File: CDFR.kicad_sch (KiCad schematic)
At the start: 11 parts, among them J1 Conn_01x03, J2 Conn_01x03, J3 Conn_01x03, J4 Conn_01x03, J5 Conn_01x03, J6 Conn_01x02_Socket, J7 Screw_Terminal_01x02, U1 RASPBERRY_PI_3_MODEL_B_, U2 YAAJ_DCDC_StepDown_LM2596

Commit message: Add files via upload
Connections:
- net GND: now also J7.2 (Pin_2), U2.2 (GND)
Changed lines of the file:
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@@
 (kicad_sch (version 20230121) (generator eeschema)
   (paper "A4")
+  (junction (at 167.64 81.28) (diameter 0) (color 0 0 0 0)
+  )
   (junction (at 60.96 73.66) (diameter 0) (color 0 0 0 0)
   )
@@
   )
   (junction (at 72.39 73.66) (diameter 0) (color 0 0 0 0)
+  )
+  (junction (at 162.56 81.28) (diameter 0) (color 0 0 0 0)
   )
   (junction (at 151.13 129.54) (diameter 0) (color 0 0 0 0)
@@
     (stroke (width 0) (type default))
   )
+  (wire (pts (xy 162.56 81.28) (xy 167.64 81.28))
+    (stroke (width 0) (type default))
+  )

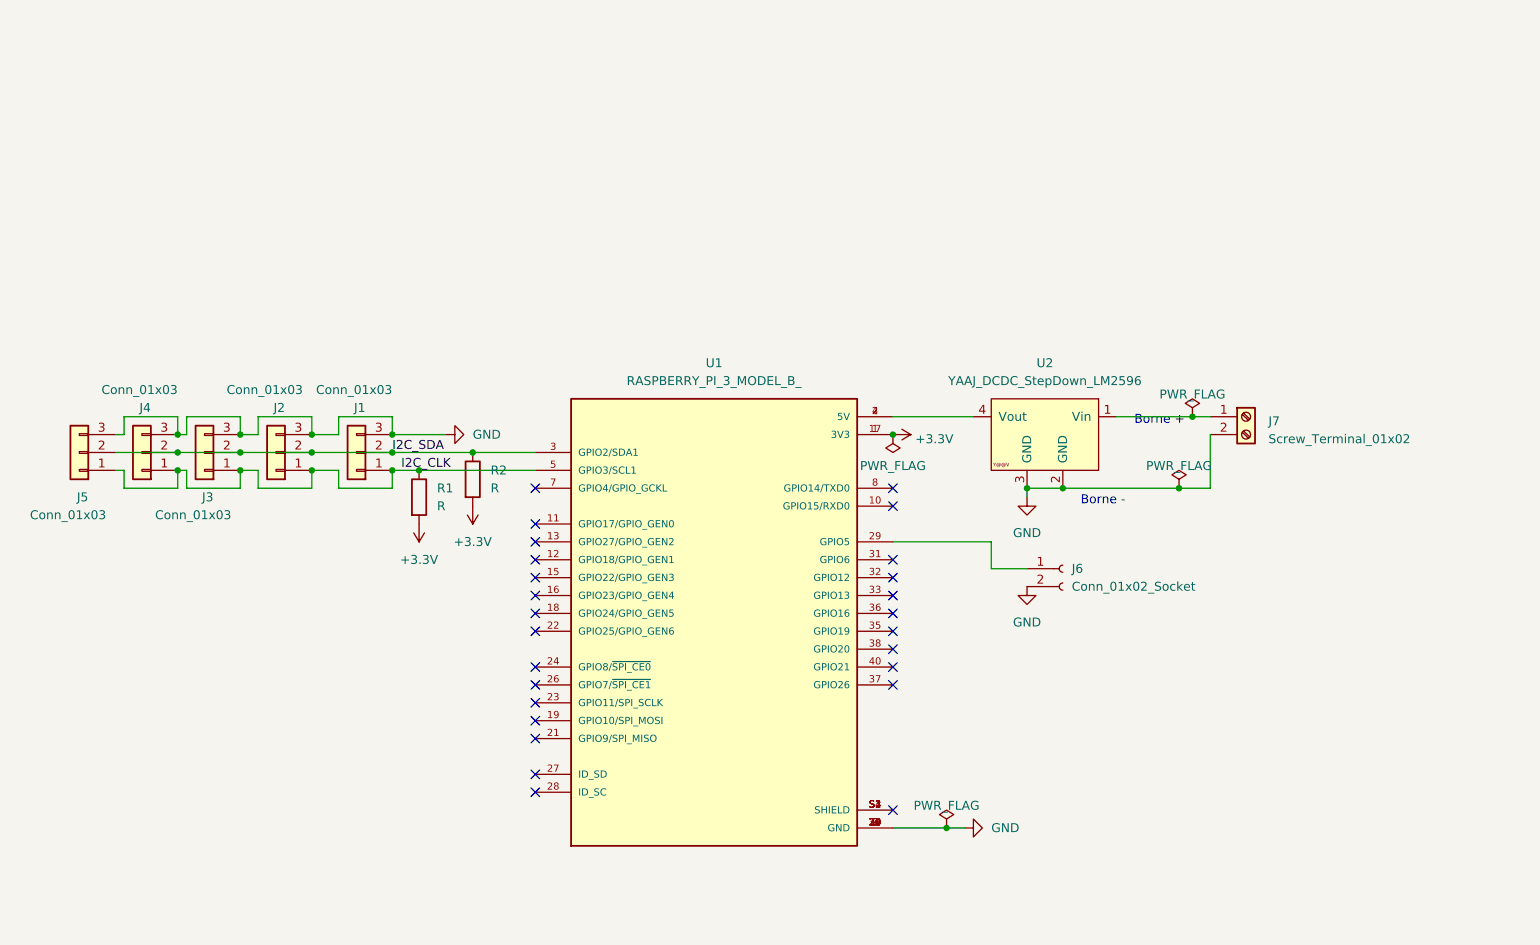
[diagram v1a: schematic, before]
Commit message: ajout lidar et antiRerse voltage
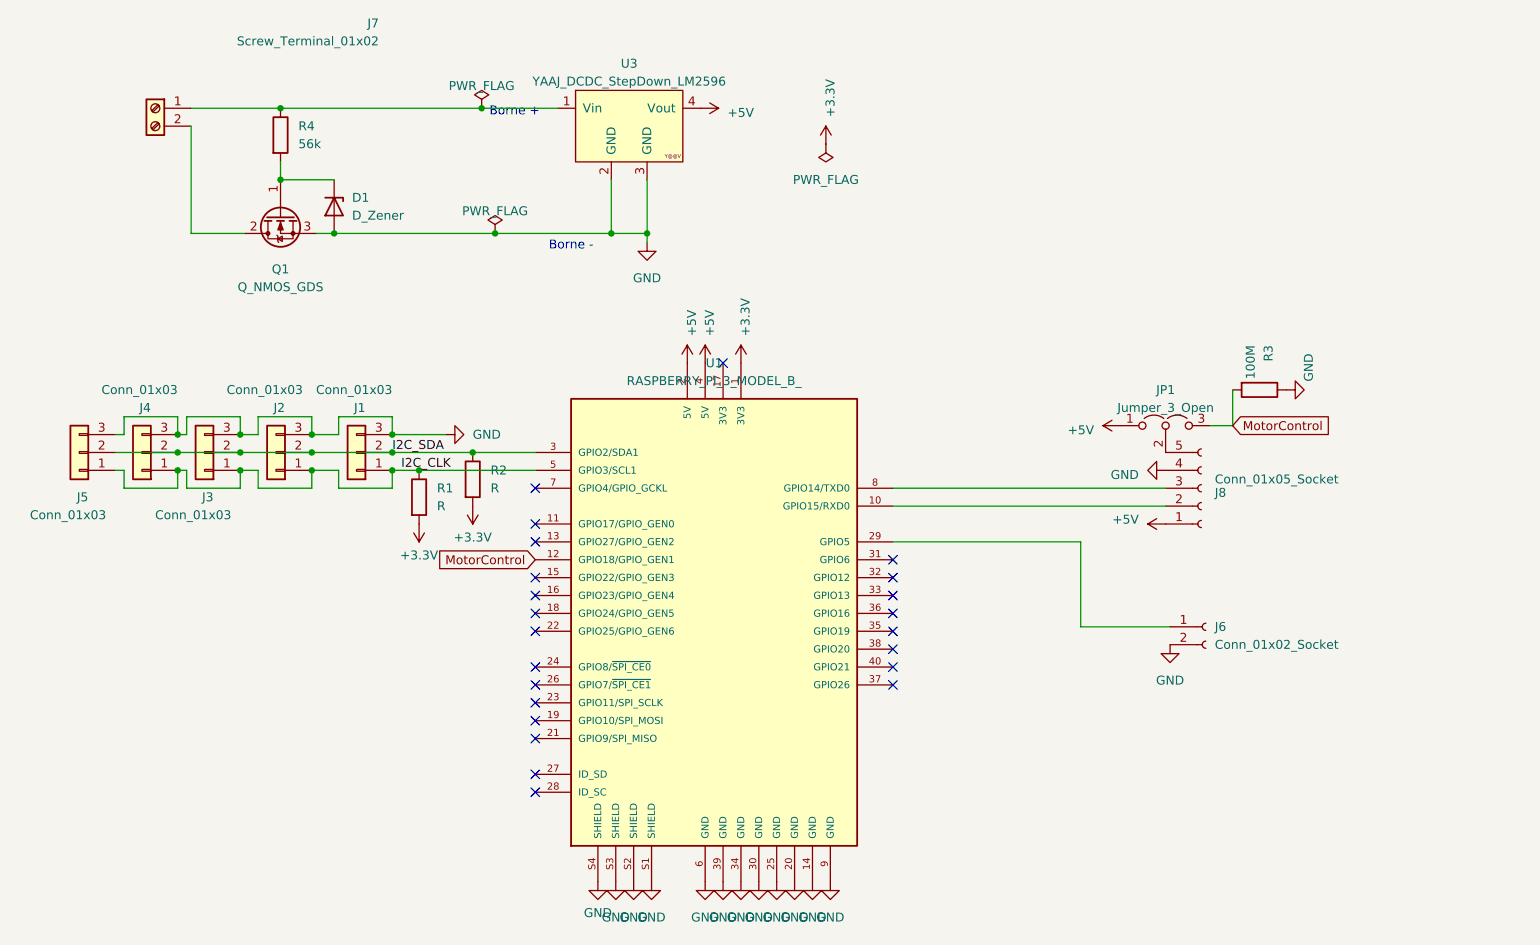
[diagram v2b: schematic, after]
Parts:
- removed U2: YAAJ_DCDC_StepDown_LM2596, emprient2:YAAJ_DCDC_StepDown_LM2596, symbol yaaj_dcdc_stepdown_lm2596:YAAJ_DCDC_StepDown_LM2596
- added D1: D_Zener, Diode_SMD:D_SOD-123, symbol Device:D_Zener
- added J8: Conn_01x05_Socket, Connector_JST:JST_XH_B5B-XH-A_1x05_P2.50mm_Vertical, symbol Connector:Conn_01x05_Socket
- added JP1: Jumper_3_Open, Connector_PinHeader_2.54mm:PinHeader_1x03_P2.54mm_Vertical, symbol Jumper:Jumper_3_Open
- added Q1: Q_NMOS_GDS, Package_TO_SOT_SMD:TO-252-2, symbol Device:Q_NMOS_GDS
- added R3: 100M, Resistor_SMD:R_0805_2012Metric, symbol Device:R
- added R4: 56k, Resistor_SMD:R_0805_2012Metric_Pad1.20x1.40mm_HandSolder, symbol Device:R
- added U3: YAAJ_DCDC_StepDown_LM2596, LM2596:YAAJ_DCDC_StepDown_LM2596, symbol yaaj_dcdc_stepdown_lm2596:YAAJ_DCDC_StepDown_LM2596
- U1: footprint emprient:MODULE_RASPBERRY_PI_3_MODEL_B_ -> raspberryPi:EmpreintPourShiel_RaspberryPi3B
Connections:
- net +3.3V: no longer U1.17 (3V3)
- net GND: now also U1.S1 (SHIELD), U1.S2 (SHIELD), U1.S3 (SHIELD), U1.S4 (SHIELD), D1.2 (A), J8.4 (Pin_4), Q1.3 (S), R3.1, U3.2 (GND), U3.3 (GND); no longer J7.2 (Pin_2)
- net at J7.1 (Pin_1): now also R4.1, U3.1 (Vin)
- net +5V: now reaches U1.2 (5V), U1.4 (5V)
- net +5V: now also J8.1 (Pin_1), JP1.1 (A), U3.4 (Vout)
- net at U1.10 (GPIO15/RXD0): now also J8.2 (Pin_2)
- net MotorControl: now reaches U1.12 (GPIO18/GPIO_GEN1)
- net MotorControl: now also JP1.3 (B), R3.2
- net at U1.8 (GPIO14/TXD0): now also J8.3 (Pin_3)
- new net: J8.5 (Pin_5), JP1.2 (C)
- new net: D1.1 (K), Q1.1 (G), R4.2
- new net: J7.2 (Pin_2), Q1.2 (D)
- no-connect marks 26 -> 23
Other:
- moved on the sheet: J6, J7

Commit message: ajout i2c power
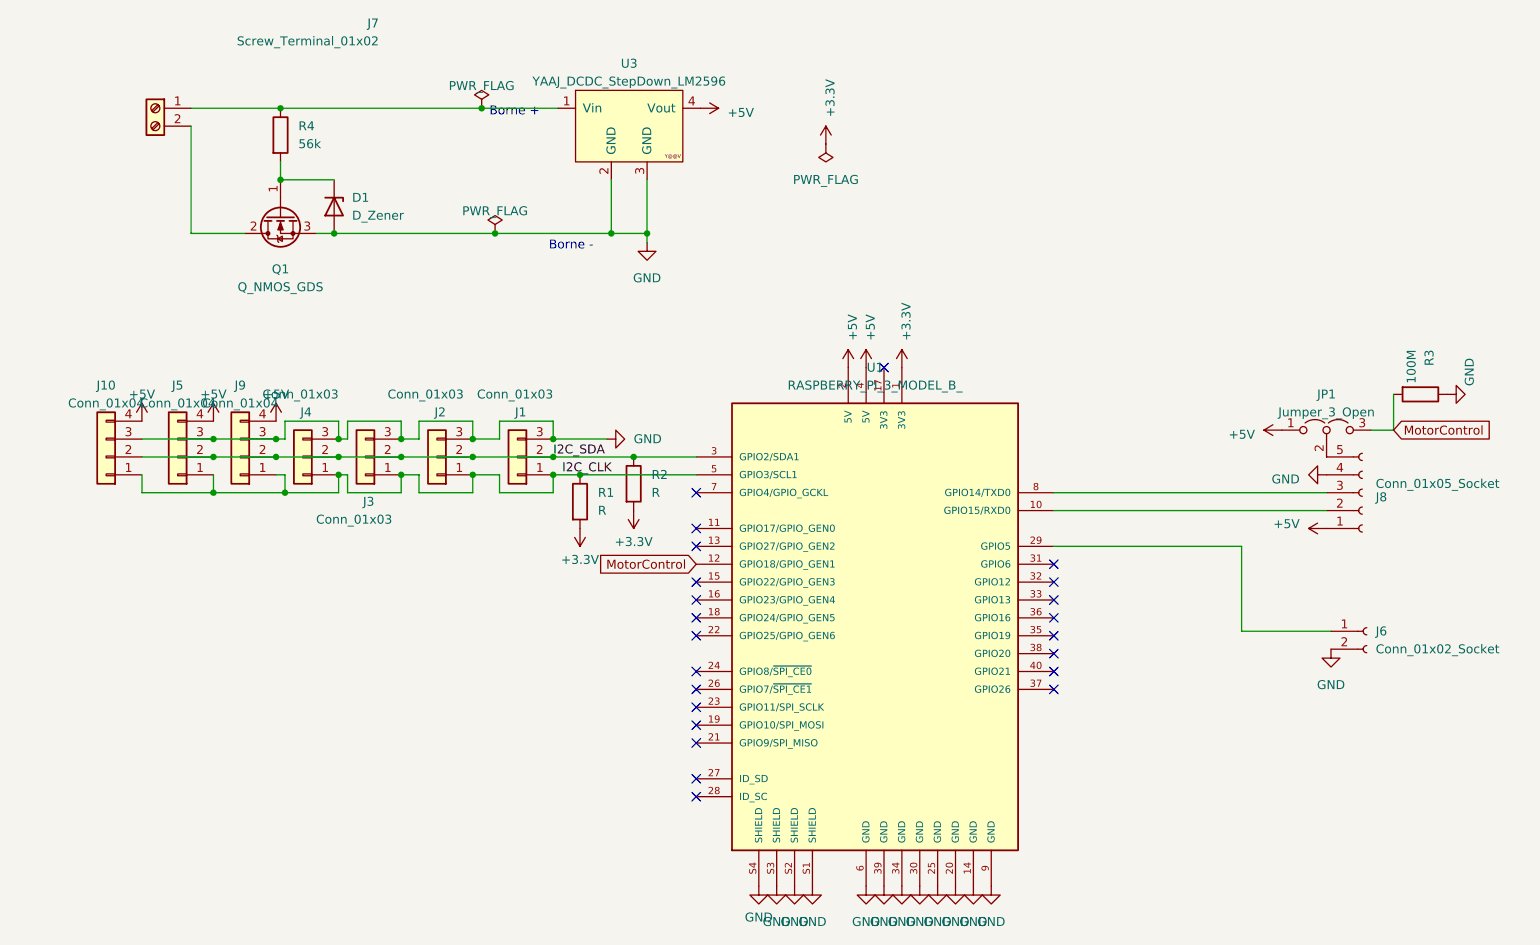
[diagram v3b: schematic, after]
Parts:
- removed J5: Conn_01x03, Connector_JST:JST_XH_B3B-XH-A_1x03_P2.50mm_Vertical, symbol Connector_Generic:Conn_01x03
- added J10, J5, J9: Conn_01x04, Connector_JST:JST_XH_B4B-XH-A_1x04_P2.50mm_Vertical, symbol Connector_Generic:Conn_01x04
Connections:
- net +5V: now also J10.4 (Pin_4), J5.4 (Pin_4), J9.4 (Pin_4)
- net GND: now also J10.3 (Pin_3), J5.3 (Pin_3), J9.3 (Pin_3)
- net I2C_CLK: now also J10.1 (Pin_1), J5.1 (Pin_1), J9.1 (Pin_1)
- net I2C_SDA: now also J10.2 (Pin_2), J5.2 (Pin_2), J9.2 (Pin_2)
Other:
- moved on the sheet: J1, J2, J3, J4, J6, J8, JP1, R1, R2, R3, U1

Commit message: Mise à jour référence
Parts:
- renumbered J10 to J10_I2C1, J1 to J1_I2C1, J2 to J2_I2C1, J3 to J3_I2C1, J4 to J4_I2C1, J5 to J5_I2C1, J8 to J8_UART0, J9 to J9_I2C1

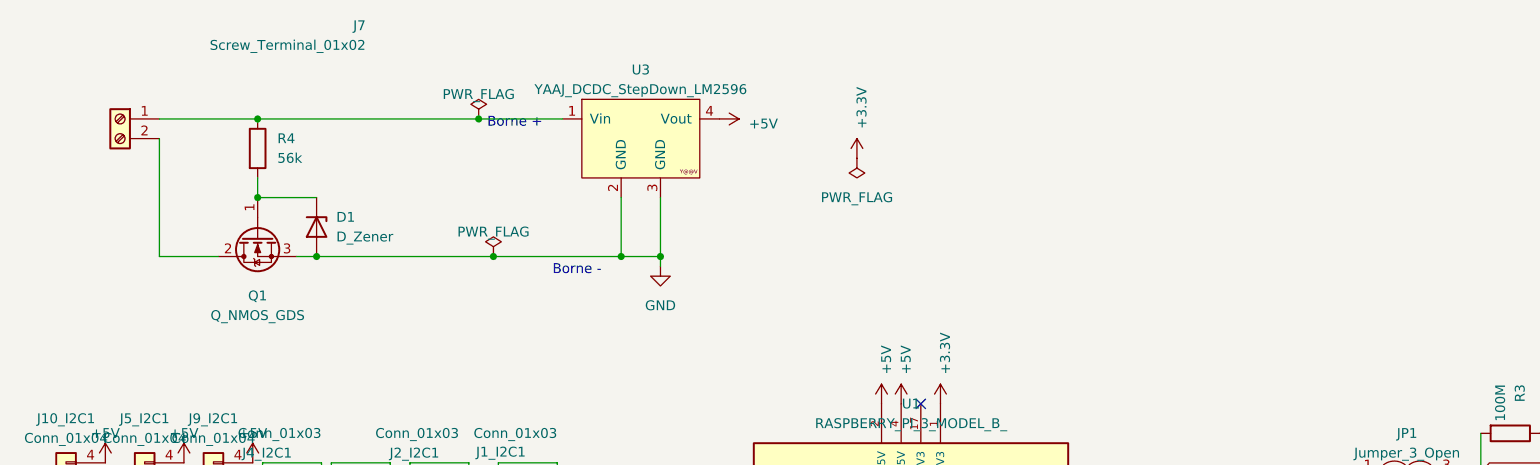
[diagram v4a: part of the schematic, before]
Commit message: TracoPower addition
Ajout traco power
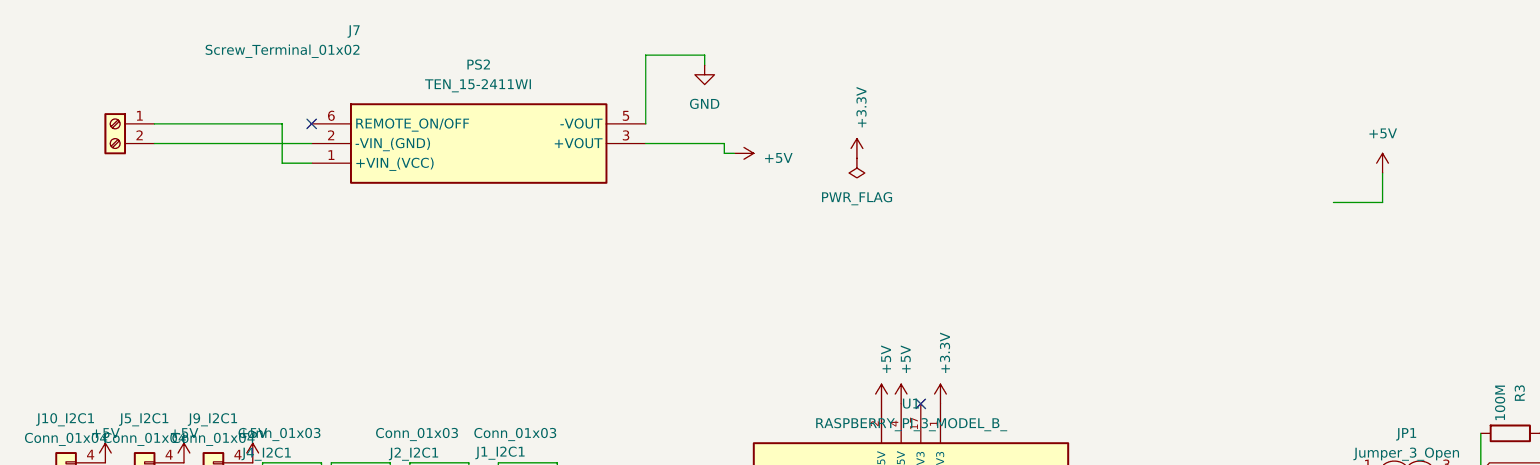
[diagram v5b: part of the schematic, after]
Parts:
- removed D1: D_Zener, Diode_SMD:D_SOD-123, symbol Device:D_Zener
- removed Q1: Q_NMOS_GDS, Package_TO_SOT_SMD:TO-252-2, symbol Device:Q_NMOS_GDS
- removed R4: 56k, Resistor_SMD:R_0805_2012Metric_Pad1.20x1.40mm_HandSolder, symbol Device:R
- removed U3: YAAJ_DCDC_StepDown_LM2596, LM2596:YAAJ_DCDC_StepDown_LM2596, symbol yaaj_dcdc_stepdown_lm2596:YAAJ_DCDC_StepDown_LM2596
- added PS2: TEN_15-2411WI, TEN152411WI, symbol SamacSys_Parts:TEN_15-2411WI
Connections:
- net +5V: now also PS2.3 (+VOUT)
- net GND: now also PS2.5 (-VOUT)
- net at J7.1 (Pin_1): now also PS2.1 (+VIN_(VCC))
- net at J7.2 (Pin_2): now also PS2.2 (-VIN_(GND))
- no-connect marks 23 -> 24
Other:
- note removed: "Borne +"
- note removed: "Borne -"
- moved on the sheet: J7

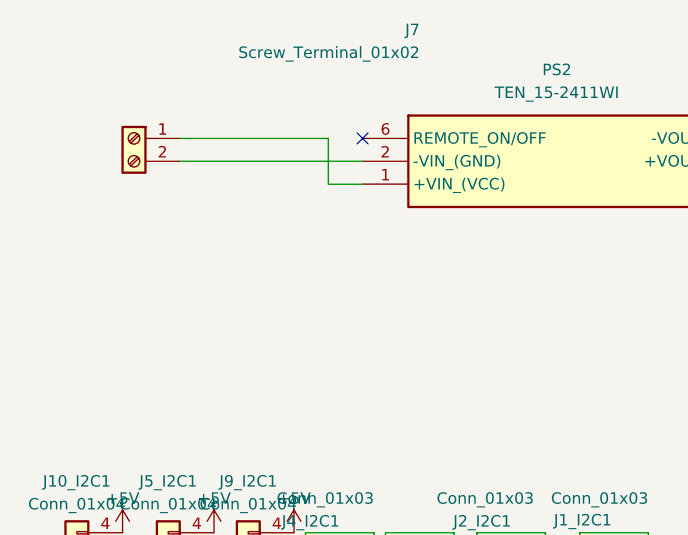
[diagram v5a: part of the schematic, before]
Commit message: Ajout porte fusible
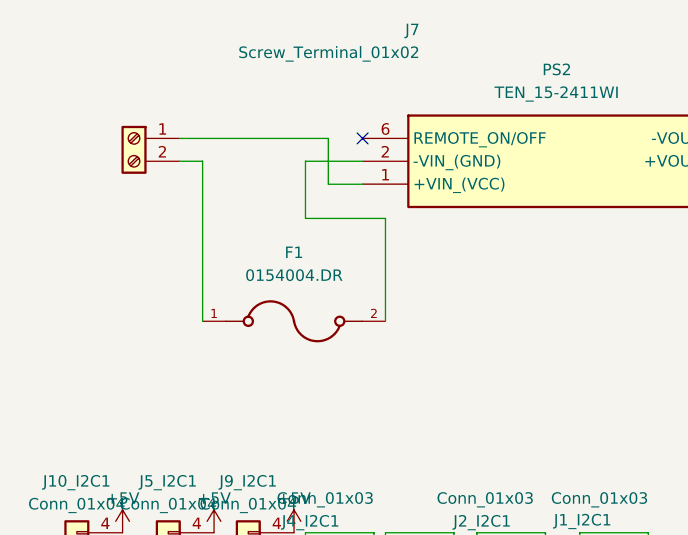
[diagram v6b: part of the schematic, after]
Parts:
- added F1: 0154004.DR, FuseHolder:FUSE_0154004.DR, symbol 0154004.DR:0154004.DR
- PS2: footprint TEN152411WI -> TEN152411:TEN152411WI
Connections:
- net at PS2.2 (-VIN_(GND)): now also F1.2; no longer J7.2 (Pin_2)
- new net: F1.1, J7.2 (Pin_2)
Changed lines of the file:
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@@
+	(wire
+		(pts
+			(xy 45.72 30.48) (xy 45.72 48.26)
+		)
+		(stroke
+			(width 0)
+			(type default)
+		)
+	)
 	(wire
 		(pts
@@
 	(wire
 		(pts
+			(xy 57.15 36.83) (xy 57.15 30.48)
+		)
+		(stroke
+			(width 0)
+			(type default)
+		)
+	)
+	(wire
+		(pts
 			(xy 114.3 19.05) (xy 114.3 20.32)
 		)
@@
 	(wire
 		(pts
-			(xy 43.18 30.48) (xy 63.5 30.48)
-		)
-		(stroke
-			(width 0)
-			(type default)
-		)
-	)
-	(wire
-		(pts
 			(xy 64.77 74.295) (xy 66.04 74.295)
 		)
@@
 	(wire
 		(pts
+			(xy 66.04 36.83) (xy 57.15 36.83)
+		)
+		(stroke
+			(width 0)
+			(type default)
+		)
+	)
+	(wire
+		(pts
 			(xy 43.18 27.94) (xy 59.69 27.94)
 		)
@@
 	(wire
 		(pts
+			(xy 57.15 30.48) (xy 63.5 30.48)
+		)
+		(stroke
+			(width 0)
+			(type default)
+		)
+	)
+	(wire
+		(pts
 			(xy 55.88 79.375) (xy 57.15 79.375)
 		)
@@
 	(wire
 		(pts
+			(xy 43.18 30.48) (xy 45.72 30.48)
+		)
+		(stroke
+			(width 0)
+			(type default)
+		)
+	)
+	(wire
+		(pts
 			(xy 83.82 79.375) (xy 87.63 79.375)
+		)
+		(stroke
+			(width 0)
+			(type default)
+		)
+	)
+	(wire
+		(pts
+			(xy 66.04 48.26) (xy 66.04 36.83)
 		)
 		(stroke
@@
 			)
 		)
-		(property "Footprint" "TEN152411WI"
+		(property "Footprint" "TEN152411:TEN152411WI"
 			(at 102.87 122.86 0)
 			(effects
@@
 					(unit 1)
 				)
+			)
+		)
+	)
+	(symbol
+		(lib_id "0154004.DR:0154004.DR")
+		(at 55.88 48.26 0)
+		(unit 1)
+		(exclude_from_sim no)
+		(in_bom yes)
+		(on_board yes)
+		(dnp no)
+		(fields_autoplaced yes)
+		(property "Reference" "F1"
+			(at 55.88 40.64 0)
+			(effects
+				(font
+					(size 1.27 1.27)
+				)
+			)
+		)
+		(property "Value" "0154004.DR"
+			(at 55.88 43.18 0)
+			(effects
+				(font
+					(size 1.27 1.27)
+				)
+			)
+		)
+		(property "Footprint" "FuseHolder:FUSE_0154004.DR"
+			(at 55.88 48.26 0)
+			(effects
+				(font
+					(size 1.27 1.27)
+				)
+				(justify bottom)
+				(hide yes)
+			)
+		)
+		(property "Datasheet" ""
+			(at 55.88 48.26 0)
+			(effects
+				(font
+					(size 1.27 1.27)
+				)
+				(hide yes)
+			)
+		)
+		(property "Description" ""
+			(at 55.88 48.26 0)
+			(effects
+				(font
+					(size 1.27 1.27)
+				)
+				(hide yes)
+			)
+		)
+		(property "MF" "Littelfuse"
+			(at 55.88 48.26 0)
+			(effects
+				(font
+					(size 1.27 1.27)
+				)
+				(justify bottom)
+				(hide yes)
+			)
+		)
+		(property "Description_1" "\nNano2 SMD FF submin fuse w/holder, 4A | Littelfuse 0154004.DR\n"
+			(at 55.88 48.26 0)
+			(effects
+				(font
+					(size 1.27 1.27)
+				)
+				(justify bottom)
+				(hide yes)
+			)
+		)
+		(property "Package" "None"
+			(at 55.88 48.26 0)
+			(effects
+				(font
+					(size 1.27 1.27)
+				)
+				(justify bottom)
+				(hide yes)
+			)
+		)
+		(property "Price" "None"
+			(at 55.88 48.26 0)
+			(effects
+				(font
+					(size 1.27 1.27)
+				)
+				(justify bottom)
+				(hide yes)
+			)
+		)
+		(property "Check_prices" "https://www.snapeda.com/parts/0154004.DR/Ersa/view-part/?ref=eda"
+			(at 55.88 48.26 0)
+			(effects
+				(font
+					(size 1.27 1.27)
+				)
+				(justify bottom)
+				(hide yes)
+			)
+		)
+		(property "SnapEDA_Link" "https://www.snapeda.com/parts/0154004.DR/Ersa/view-part/?ref=snap"
+			(at 55.88 48.26 0)
+			(effects
+				(font
+					(size 1.27 1.27)
+				)
+				(justify bottom)
+				(hide yes)
+			)
+		)
+		(property "MP" "0154004.DR"
+			(at 55.88 48.26 0)
+			(effects
+				(font
+					(size 1.27 1.27)
+				)
+				(justify bottom)
+				(hide yes)
+			)
+		)
+		(property "Availability" "In Stock"
+			(at 55.88 48.26 0)
+			(effects
+				(font
+					(size 1.27 1.27)
+				)
+				(justify bottom)
+				(hide yes)
+			)
+		)
+		(property "MANUFACTURER" "Littelfuse"
+			(at 55.88 48.26 0)
+			(effects
+				(font
+					(size 1.27 1.27)
+				)
+				(justify bottom)
+				(hide yes)
+			)
+		)
+		(pin "1"
+		)
+		(pin "2"
+		)
+		(instances
+			(project ""
+				(path "/4baf3cc7-e737-4c25-a00c-bc79957d9384"
+					(reference "F1")
+					(unit 1)
+				)
